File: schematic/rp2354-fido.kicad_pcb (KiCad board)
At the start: 2 copper layers, 41.8 x 18 mm, 40 parts, among them J1 USB_C_Receptacle_USB2.0_14P, J2 Conn_01x03_Pin, SW1 SW_Push_Dual, U1 RP2354A, U2 AP2112K-3.3, U3 USBLC6-2SC6, Y1 Crystal_Small

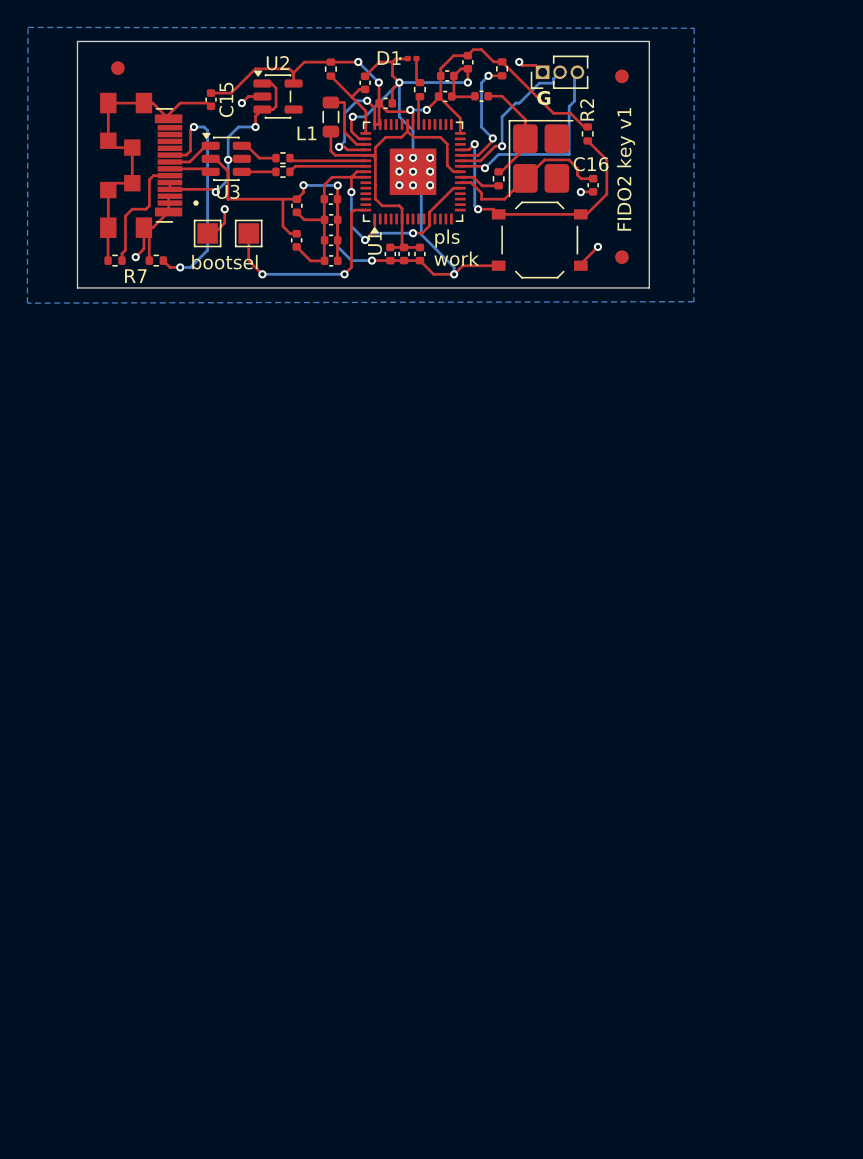
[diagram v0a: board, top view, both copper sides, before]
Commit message: new usb c plug, bootsel switch added
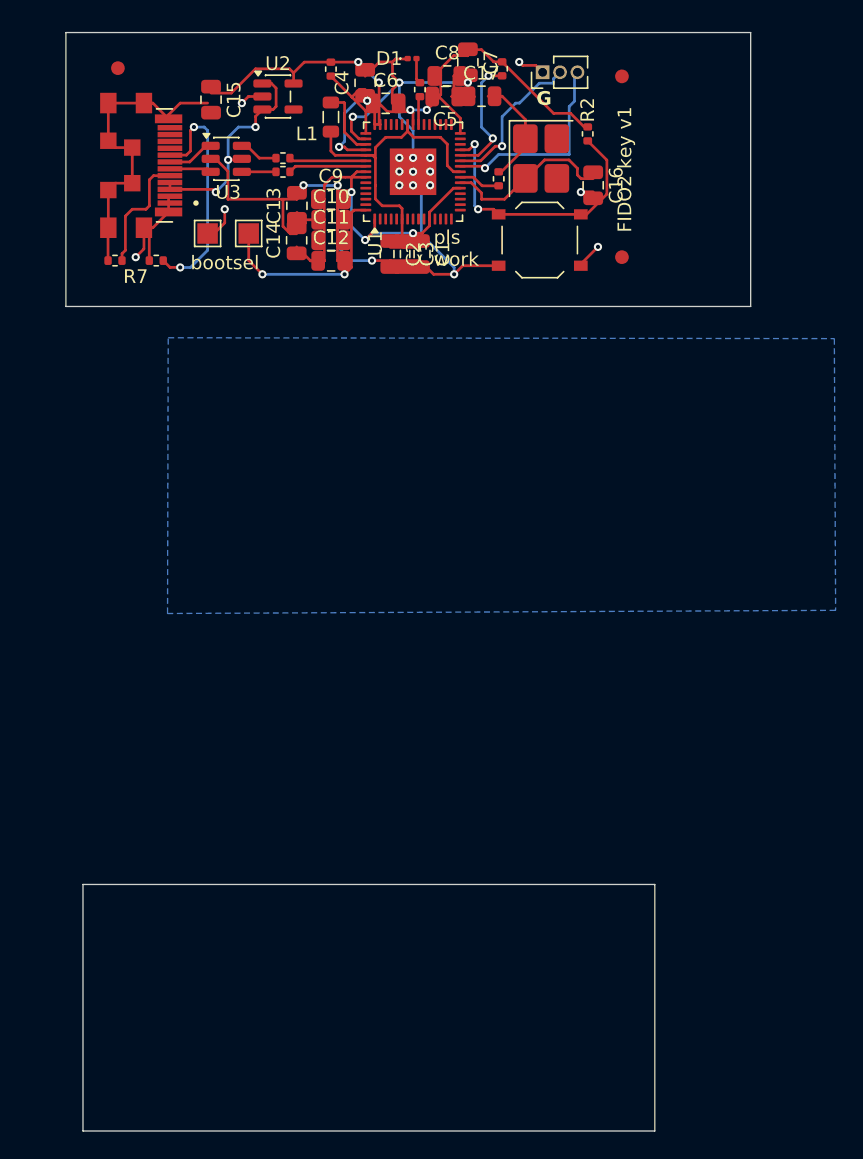
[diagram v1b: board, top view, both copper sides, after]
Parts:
- C1, C10, C11, C12, C13, C14, C15, C16, C17, C2, C3, C4, C5, C6, C7, C8, C9: footprint Capacitor_SMD:C_0402_1005Metric -> Capacitor_SMD:C_0805_2012Metric
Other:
- board size 41.8 x 18 mm -> 50 x 80.2 mm
